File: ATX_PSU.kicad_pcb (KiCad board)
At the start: 4 copper layers, 100 x 100 mm, 179 parts, among them J200 09031967921, J400 15246040, J401 Conn_01x06_Pin, J402 ATX-24, J800 USB_C_Receptacle_USB2.0_16P, Q404 AO3400A, Q409 AO3400A, Q410 HSBA8119, Q415 MMBT5551, Q416 AO3400A, Q417 HSBA8119, Q700 MMST3904, SW401 SW_SPDT, U100 W25Q128, U302 CH334P, U400 INA219AIDCNR, U401 TPD2E2U06DCK, U402 TPD2E2U06DCK, U405 STM32H562VGTx, U407 INA219AIDCNR, U408 INA219AIDCNR, U500 TJA1044GTK_3Z, U600 TJA1044GTK_3Z, U700 STM32F103CBTx, U801 FSUSB42UMX, X300 Q13FC1350000400, Y400 ASE-xxxMHz, Y700 8 MHz, Y900 12Mhz

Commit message: finished PCB
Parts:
- moved D400 6.63 mm to (51.9, 54.8)
- moved R405 6.55 mm to (51.9, 57.8)
- moved D406 5.65 mm to (54.9, 54.8)
- moved R407 5.56 mm to (54.9, 57.8)
- moved SW401 4.00 mm to (86.4, 52.8)
- moved D412 3.66 mm to (77.9, 54.8)
- moved R444 3.55 mm to (77.9, 57.8)
- moved D405 3.27 mm to (59.4, 54.8)
- moved R406 3.10 mm to (59.4, 57.8)
- moved D407 2.50 mm to (62.4, 55.0)
- moved D411 2.27 mm to (74.4, 54.8)
- moved R408 2.15 mm to (62.4, 57.8)
- moved R433 2.08 mm to (74.4, 57.8)
- moved D410 1.47 mm to (71.4, 54.8)
- moved D409 1.38 mm to (65.9, 54.8)
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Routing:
- net /ATX connector/+5V_ATX: track 118.7 -> 175.4 mm, vias 1 -> 2
- net /ATX connector/+3.3V_ATX: track 87.1 -> 106.9 mm
- net /ATX connector/-12V_ATX: track 37.9 -> 31.9 mm, vias 3 -> 1
- net +5V_SB: track 215.4 -> 211.9 mm
- net GND: track 132.1 -> 135.4 mm, vias 85 -> 83
- net +5V: track 219.0 -> 216.7 mm
- net /ATX connector/PS_ON#_ATX: track 57.1 -> 59.2 mm
- net +24V: track 97.1 -> 98.1 mm
- net Net-(D407-Pad1): track 2.21 -> 1.50 mm
- net Net-(D412-Pad1): track 2.21 -> 1.71 mm
- net Net-(D411-Pad1): track 2.21 -> 1.71 mm
- net Net-(D410-Pad1): track 2.21 -> 1.71 mm
- net Net-(D409-Pad2): track 2.21 -> 1.71 mm
- net Net-(D406-Pad1): track 2.21 -> 1.71 mm
- net Net-(D405-Pad1): track 2.21 -> 1.71 mm
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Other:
- board text added: "-12V"
- board text added: "12V"
- board text added: "24V"
- board text added: "3.3V"
- board text added: "5V"
- board text added: "5V_SB"

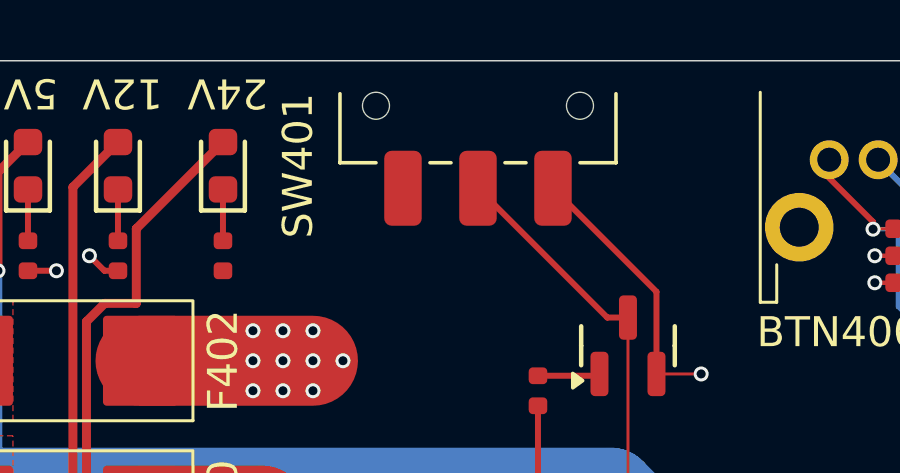
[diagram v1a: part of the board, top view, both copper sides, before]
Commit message: updated LED resistor values
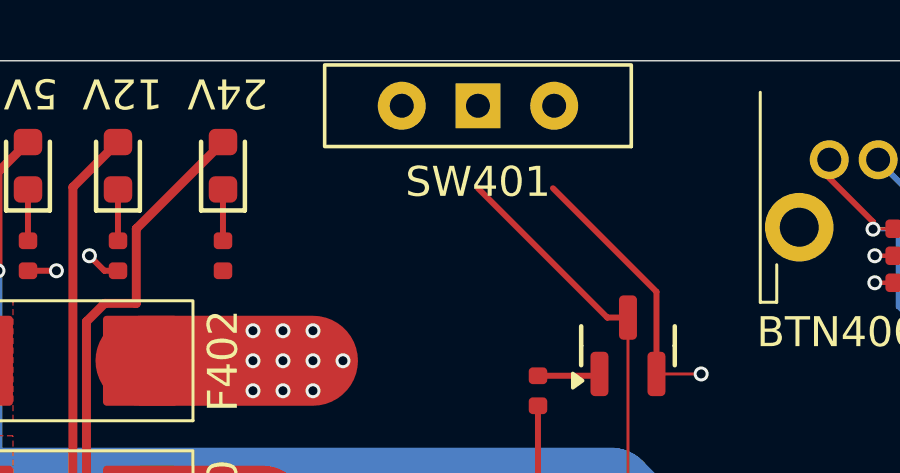
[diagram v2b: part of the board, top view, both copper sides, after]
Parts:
- R405: value 10kΩ -> 220
- R406, R407: value 10kΩ -> 560
- R408, R431, R433: value 10kΩ -> 2.2k
- R432: value 10kΩ -> 260
- R444: value 10kΩ -> 4.7k
- SW401: footprint Button_Switch_SMD:SW_SPDT_CK_JS102011SAQN -> Button_Switch_THT:SW_Slide-03_Wuerth-WS-SLTV_10x2.5x6.4_P2.54mm
